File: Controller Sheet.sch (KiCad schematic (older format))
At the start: 20 parts, among them J1 USB_B_Micro, U1 ATSAMD11D14A-SS, Y1 Crystal_GND2

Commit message: Fixed PISO Shift Register Wiring
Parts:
- removed U?: 74HC596, symbol 74xx:74HC596
- removed U?: ADP7142AUJZ-3.3, Package_TO_SOT_SMD:TSOT-23-5, symbol Regulator_Linear:ADP7142AUJZ-3.3
- added U?: AP2138N-3.3TRG1, Package_TO_SOT_SMD:SOT-23_Handsoldering, symbol Library:AP2138N-3.3TRG1
- added U?: 74HC595D_118, digikey-footprints:SOIC-16_W3.90mm, symbol dk_Logic-Shift-Registers:74HC595D_118
- C1, C2, C? (x2): footprint (none) -> Capacitor_SMD:C_1206_3216Metric_Pad1.42x1.75mm_HandSolder
- C?: value 4.7u -> 1u; footprint (none) -> Capacitor_SMD:C_1206_3216Metric_Pad1.42x1.75mm_HandSolder
- C?: value 1n -> 1u; footprint (none) -> Capacitor_SMD:C_1206_3216Metric_Pad1.42x1.75mm_HandSolder
- J1: footprint (none) -> Connector_USB:USB_Micro-B_Molex_47346-0001
- J?: footprint (none) -> Connector_PinHeader_2.54mm:PinHeader_2x04_P2.54mm_Vertical
- J?: footprint (none) -> Connector_PinHeader_1.00mm:PinHeader_1x04_P1.00mm_Vertical
- R? (x3): footprint (none) -> Resistor_SMD:R_1206_3216Metric_Pad1.42x1.75mm_HandSolder
- RV?: footprint (none) -> Potentiometer_THT:Potentiometer_Runtron_RM-065_Vertical
- SW?: footprint (none) -> Button_Switch_THT:SW_PUSH_6mm
- Y1: footprint (none) -> Crystal:Crystal_SMD_SeikoEpson_MC146-4Pin_6.7x1.5mm_HandSoldering; symbol Device:Crystal_GND2 -> Device:Crystal_GND23
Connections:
- net +3V3: now also U?.16 (VCC), U?.2 (OUT)
- net +5V: now also U?.3 (IN)
- net GND: now also U?.1 (GND), U?.13 (OE), U?.8 (GND); no longer Y1.2
- net Lock LEDS/CAPS_LOCK: now also U?.1 (Q1)
- net Lock LEDS/NUM_LOCK: now also U?.15 (Q0)
- net Lock LEDS/SCROLL_LOCK: now also U?.2 (Q2)
- net OUT_SHIFT_0_DATA: now also U?.14 (DS)
- net OUT_SHIFT_RCLK: now also U?.12 (STCP)
- net RESET: now also U?.10 (MR)
- net SHIFT_CLK: now also U?.11 (SHCP)
- net at C4.1, U1.4 (PA08/XIN): now also Y1.4; no longer Y1.3
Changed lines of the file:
@@
 F 0 "J1" H 1657 5067 50  0000 C CNN
 F 1 "USB_B_Micro" H 1657 4976 50  0000 C CNN
-F 2 "" H 1750 4550 50  0001 C CNN
+F 2 "Connector_USB:USB_Micro-B_Molex_47346-0001" H 1750 4550 50  0001 C CNN
 F 3 "~" H 1750 4550 50  0001 C CNN
 	1    1600 4600
@@
 F 0 "C1" H 5715 2796 50  0000 L CNN
 F 1 "100n" H 5715 2705 50  0000 L CNN
-F 2 "" H 5638 2600 50  0001 C CNN
+F 2 "Capacitor_SMD:C_1206_3216Metric_Pad1.42x1.75mm_HandSolder" H 5638 2600 50  0001 C CNN
 F 3 "~" H 5600 2750 50  0001 C CNN
 	1    5600 2750
@@
 F 0 "C2" H 5215 2796 50  0000 L CNN
 F 1 "4.7u" H 5215 2705 50  0000 L CNN
-F 2 "" H 5138 2600 50  0001 C CNN
+F 2 "Capacitor_SMD:C_1206_3216Metric_Pad1.42x1.75mm_HandSolder" H 5138 2600 50  0001 C CNN
 F 3 "~" H 5100 2750 50  0001 C CNN
 	1    5100 2750
@@
 	6750 4300 6750 2600
 $Comp
-L Device:Crystal_GND2 Y1
+L Device:Crystal_GND23 Y1
 U 1 1 5E8CA600
 P 7750 3000
-F 0 "Y1" H 7750 3268 50  0000 C CNN
-F 1 "Crystal_GND2" H 7750 3177 50  0000 C CNN
-F 2 "" H 7750 3000 50  0001 C CNN
+F 0 "Y1" H 7750 3268 50  0000 L CNN
+F 1 "Crystal_GND2" H 7750 3177 50  0000 L CNN
+F 2 "Crystal:Crystal_SMD_SeikoEpson_MC146-4Pin_6.7x1.5mm_HandSoldering" H 7750 3000 50  0001 C CNN
 F 3 "~" H 7750 3000 50  0001 C CNN
 	1    7750 3000
@@
 	8150 3400 7750 3400
 Wire Wire Line
-	7750 3200 7750 3400
-Wire Wire Line
 	7750 3400 7750 3500
 $Comp
@@
 F 0 "SW?" H 10300 4335 50  0000 C CNN
 F 1 "SW_Push" H 10300 4244 50  0000 C CNN
-F 2 "" H 10300 4250 50  0001 C CNN
+F 2 "Button_Switch_THT:SW_PUSH_6mm" H 10300 4250 50  0001 C CNN
 F 3 "~" H 10300 4250 50  0001 C CNN
 	1    10300 4050
@@
 F 0 "R?" H 9270 3546 50  0000 L CNN
 F 1 "100K" H 9270 3455 50  0000 L CNN
-F 2 "" V 9130 3500 50  0001 C CNN
+F 2 "Resistor_SMD:R_1206_3216Metric_Pad1.42x1.75mm_HandSolder" V 9130 3500 50  0001 C CNN
 F 3 "~" H 9200 3500 50  0001 C CNN
 	1    9200 3500
@@
 F 0 "C?" H 9315 4096 50  0000 L CNN
 F 1 "4.7n" H 9315 4005 50  0000 L CNN
-F 2 "" H 9238 3900 50  0001 C CNN
+F 2 "Capacitor_SMD:C_1206_3216Metric_Pad1.42x1.75mm_HandSolder" H 9238 3900 50  0001 C CNN
 F 3 "~" H 9200 4050 50  0001 C CNN
 	1    9200 4050
@@
 F 0 "R?" V 9543 3800 50  0000 C CNN
 F 1 "39" V 9634 3800 50  0000 C CNN
-F 2 "" V 9680 3800 50  0001 C CNN
+F 2 "Resistor_SMD:R_1206_3216Metric_Pad1.42x1.75mm_HandSolder" V 9680 3800 50  0001 C CNN
 F 3 "~" H 9750 3800 50  0001 C CNN
 	1    9750 3800
@@
 F 0 "J?" H 9850 6167 50  0000 C CNN
 F 1 "DEBUG" H 9850 6076 50  0000 C CNN
-F 2 "" H 9800 5750 50  0001 C CNN
+F 2 "Connector_PinHeader_2.54mm:PinHeader_2x04_P2.54mm_Vertical" H 9800 5750 50  0001 C CNN
 F 3 "~" H 9800 5750 50  0001 C CNN
 	1    9800 5750
@@
 OUT_SHIFT_0_DATA
 Wire Wire Line
-	4750 3600 4750 3100
-Wire Wire Line
 	4750 3600 5550 3600
 Wire Wire Line
@@
 F 0 "R?" H 8770 4096 50  0000 L CNN
 F 1 "39" H 8770 4005 50  0000 L CNN
-F 2 "" V 8630 4050 50  0001 C CNN
+F 2 "Resistor_SMD:R_1206_3216Metric_Pad1.42x1.75mm_HandSolder" V 8630 4050 50  0001 C CNN
 F 3 "~" H 8700 4050 50  0001 C CNN
 	1    8700 4050
@@
 P 2900 6150
 F 0 "C?" H 3015 6196 50  0000 L CNN
-F 1 "4.7u" H 3015 6105 50  0000 L CNN
-F 2 "" H 2938 6000 50  0001 C CNN
+F 1 "1u" H 3015 6105 50  0000 L CNN
+F 2 "Capacitor_SMD:C_1206_3216Metric_Pad1.42x1.75mm_HandSolder" H 2938 6000 50  0001 C CNN
 F 3 "~" H 2900 6150 50  0001 C CNN
 	1    2900 6150
 	1    0    0    -1
 $EndComp
-$Comp
-L 74xx:74HC596 U?
-U 1 1 5E946AE2
-P 2850 3300
-F 0 "U?" H 2850 4081 50  0000 C CNN
-F 1 "74HC596" H 2850 3990 50  0000 C CNN
-F 2 "" H 2850 3300 50  0001 C CNN
-F 3 "https://assets.nexperia.com/documents/data-sheet/74HC_HCT595.pdf" H 2850 3300 50  0001 C CNN
-	1    2850 3300
-	-1   0    0    -1
-$EndComp
-Wire Wire Line
-	3250 3100 4750 3100
-Wire Wire Line
-	3950 3400 3250 3400
 Wire Wire Line
 	3950 4400 5550 4400
 Wire Wire Line
-	3850 2900 3250 2900
-Wire Wire Line
 	3850 4500 5550 4500
-Wire Wire Line
-	3250 3500 3500 3500
 $Comp
 L power:GND #PWR?
@@
 $EndComp
 Wire Wire Line
-	3500 3500 3500 4100
-Wire Wire Line
-	2850 4000 2850 4100
-Wire Wire Line
 	2850 4100 3500 4100
 Connection ~ 3500 4100
@@
 F 0 "C?" H 3615 2596 50  0000 L CNN
 F 1 "100n" H 3615 2505 50  0000 L CNN
-F 2 "" H 3538 2400 50  0001 C CNN
+F 2 "Capacitor_SMD:C_1206_3216Metric_Pad1.42x1.75mm_HandSolder" H 3538 2400 50  0001 C CNN
 F 3 "~" H 3500 2550 50  0001 C CNN
 	1    3500 2550
@@
 	2850 2400 3500 2400
 Wire Wire Line
-	3500 2700 3500 3500
-Connection ~ 3500 3500
+	3500 2700 3500 3400
 Wire Wire Line
 	2850 2400 2850 2300
@@
 F 0 "J?" H 1518 5475 50  0000 C CNN
 F 1 "Conn_01x04" H 1518 5566 50  0000 C CNN
-F 2 "" H 1600 5900 50  0001 C CNN
+F 2 "Connector_PinHeader_1.00mm:PinHeader_1x04_P1.00mm_Vertical" H 1600 5900 50  0001 C CNN
 F 3 "~" H 1600 5900 50  0001 C CNN
 	1    1600 5900
@@
 SHIFT_CLK
 Wire Wire Line
-	3950 4400 3950 3400
-Wire Wire Line
-	3850 4500 3850 2900
-Wire Wire Line
-	3250 3200 4850 3200
+	3850 4500 3850 3500
 Wire Wire Line
 	4750 1900 10250 1900
-Connection ~ 4750 3100
 Wire Wire Line
 	4050 4300 4050 1900
@@
 $EndSheet
 Wire Wire Line
-	2450 2900 2100 2900
-Wire Wire Line
-	2450 3000 2100 3000
-Wire Wire Line
-	2450 3100 2100 3100
-$Comp
-L Regulator_Linear:ADP7142AUJZ-3.3 U?
-U 1 1 5EB29370
-P 3500 5800
-F 0 "U?" H 3500 6167 50  0000 C CNN
-F 1 "ADP7142AUJZ-3.3" H 3500 6076 50  0000 C CNN
-F 2 "Package_TO_SOT_SMD:TSOT-23-5" H 3500 5400 50  0001 C CIN
-F 3 "https://www.analog.com/media/en/technical-documentation/data-sheets/ADP7142.pdf" H 3500 5300 50  0001 C CNN
-	1    3500 5800
-	1    0    0    -1
-$EndComp
-Wire Wire Line
 	2150 5700 2900 5700
 Connection ~ 2150 5700
-Wire Wire Line
-	3100 5900 2900 5900
-Wire Wire Line
-	2900 5900 2900 5700
 Connection ~ 2900 5700
 Wire Wire Line
 	2900 5700 3100 5700
-Wire Wire Line
-	2900 5900 2900 6000
-Connection ~ 2900 5900
 Wire Wire Line
 	3500 6100 3500 6300
@@
 Wire Wire Line
 	4100 5500 4100 5700
-Wire Wire Line
-	3900 5800 4100 5800
-Wire Wire Line
-	4100 5800 4100 5700
 Connection ~ 4100 5700
 $Comp
@@
 P 4100 6150
 F 0 "C?" H 4215 6196 50  0000 L CNN
-F 1 "1n" H 4215 6105 50  0000 L CNN
-F 2 "" H 4138 6000 50  0001 C CNN
+F 1 "1u" H 4215 6105 50  0000 L CNN
+F 2 "Capacitor_SMD:C_1206_3216Metric_Pad1.42x1.75mm_HandSolder" H 4138 6000 50  0001 C CNN
 F 3 "~" H 4100 6150 50  0001 C CNN
 	1    4100 6150
 	1    0    0    -1
 $EndComp
-Wire Wire Line
-	4100 5800 4100 6000
-Connection ~ 4100 5800
 $Comp
 L power:GND #PWR?
@@
 Wire Wire Line
 	4650 1800 4650 3700
-Wire Wire Line
-	4750 1900 4750 3100
 Connection ~ 8700 2000
 Wire Wire Line
 	8700 2000 8700 3800
 Wire Wire Line
-	4850 2000 4850 3200
+	4850 2000 4850 3100
 $Comp
 L power:GND #PWR?
@@
 F 0 "RV?" V 7543 1200 50  0000 C CNN
 F 1 "R_POT" V 7634 1200 50  0000 C CNN
-F 2 "" H 7750 1200 50  0001 C CNN
+F 2 "Potentiometer_THT:Potentiometer_Runtron_RM-065_Vertical" H 7750 1200 50  0001 C CNN
 F 3 "~" H 7750 1200 50  0001 C CNN
 	1    7750 1200
@@
 	7500 1500 9250 1500
 Connection ~ 9250 1500
+$Comp
+L Library:AP2138N-3.3TRG1 U?
+U 1 1 5E99716C
+P 3500 5800
+F 0 "U?" H 3500 6167 50  0000 C CNN
+F 1 "AP2138N-3.3TRG1" H 3500 6076 50  0000 C CNN
+F 2 "Package_TO_SOT_SMD:SOT-23_Handsoldering" H 4450 5500 50  0001 C CNN
+F 3 "https://www.diodes.com/assets/Datasheets/AP2138-9.pdf" H 3500 6150 50  0001 C CNN
+	1    3500 5800
+	1    0    0    -1
+$EndComp
+Wire Wire Line
+	2900 5700 2900 6000
+Wire Wire Line
+	4100 5700 4100 6000
+$Comp
+L dk_Logic-Shift-Registers:74HC595D_118 U?
+U 1 1 5E9A4DAC
+P 2850 2800
+F 0 "U?" H 2900 3103 60  0000 C CNN
+F 1 "74HC595D_118" H 2900 2997 60  0000 C CNN
+F 2 "digikey-footprints:SOIC-16_W3.90mm" H 3050 3000 60  0001 L CNN
+F 3 "https://assets.nexperia.com/documents/data-sheet/74HC_HCT595.pdf" H 3050 3100 60  0001 L CNN
+F 4 "1727-2821-1-ND" H 3050 3200 60  0001 L CNN "Digi-Key_PN"
+F 5 "74HC595D,118" H 3050 3300 60  0001 L CNN "MPN"
+F 6 "Integrated Circuits (ICs)" H 3050 3400 60  0001 L CNN "Category"
+F 7 "Logic - Shift Registers" H 3050 3500 60  0001 L CNN "Family"
+F 8 "https://assets.nexperia.com/documents/data-sheet/74HC_HCT595.pdf" H 3050 3600 60  0001 L CNN "DK_Datasheet_Link"
+F 9 "/product-detail/en/nexperia-usa-inc/74HC595D,118/1727-2821-1-ND/763394" H 3050 3700 60  0001 L CNN "DK_Detail_Page"
+F 10 "IC SHIFT REGISTER 8BIT 16SOIC" H 3050 3800 60  0001 L CNN "Description"
+F 11 "Nexperia USA Inc." H 3050 3900 60  0001 L CNN "Manufacturer"
+F 12 "Active" H 3050 4000 60  0001 L CNN "Status"
+	1    2850 2800
+	-1   0    0    -1
+$EndComp
+Wire Wire Line
+	2850 3900 2850 4100
+Wire Wire Line
+	2350 2900 2100 2900
+Wire Wire Line
+	2350 3000 2100 3000
+Wire Wire Line
+	2350 3100 2100 3100
+Wire Wire Line
+	4750 1900 4750 3200
+Wire Wire Line
+	3250 3100 4850 3100
+Wire Wire Line
+	3250 3200 4750 3200
+Connection ~ 4750 3200
+Wire Wire Line
+	4750 3200 4750 3600
+Wire Wire Line
+	3250 3300 3950 3300
+Wire Wire Line
+	3950 3300 3950 4400
+Wire Wire Line
+	3250 3400 3500 3400
+Connection ~ 3500 3400
+Wire Wire Line
+	3500 3400 3500 4100
+Wire Wire Line
+	3250 3500 3850 3500
 $EndSCHEMATC

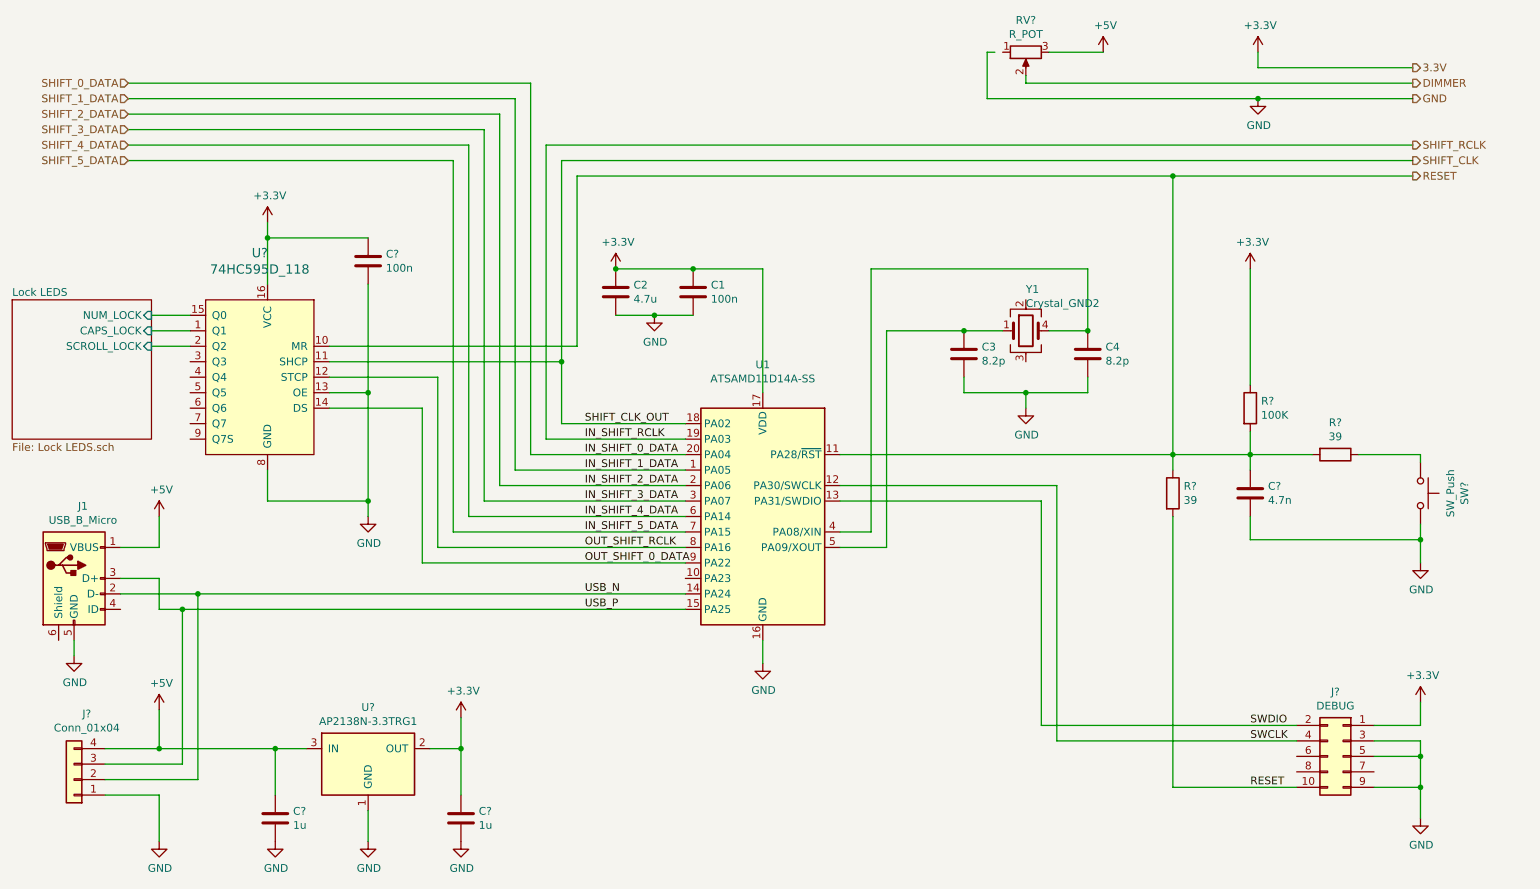
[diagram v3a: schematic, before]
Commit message: Corrected errors found in design rule check
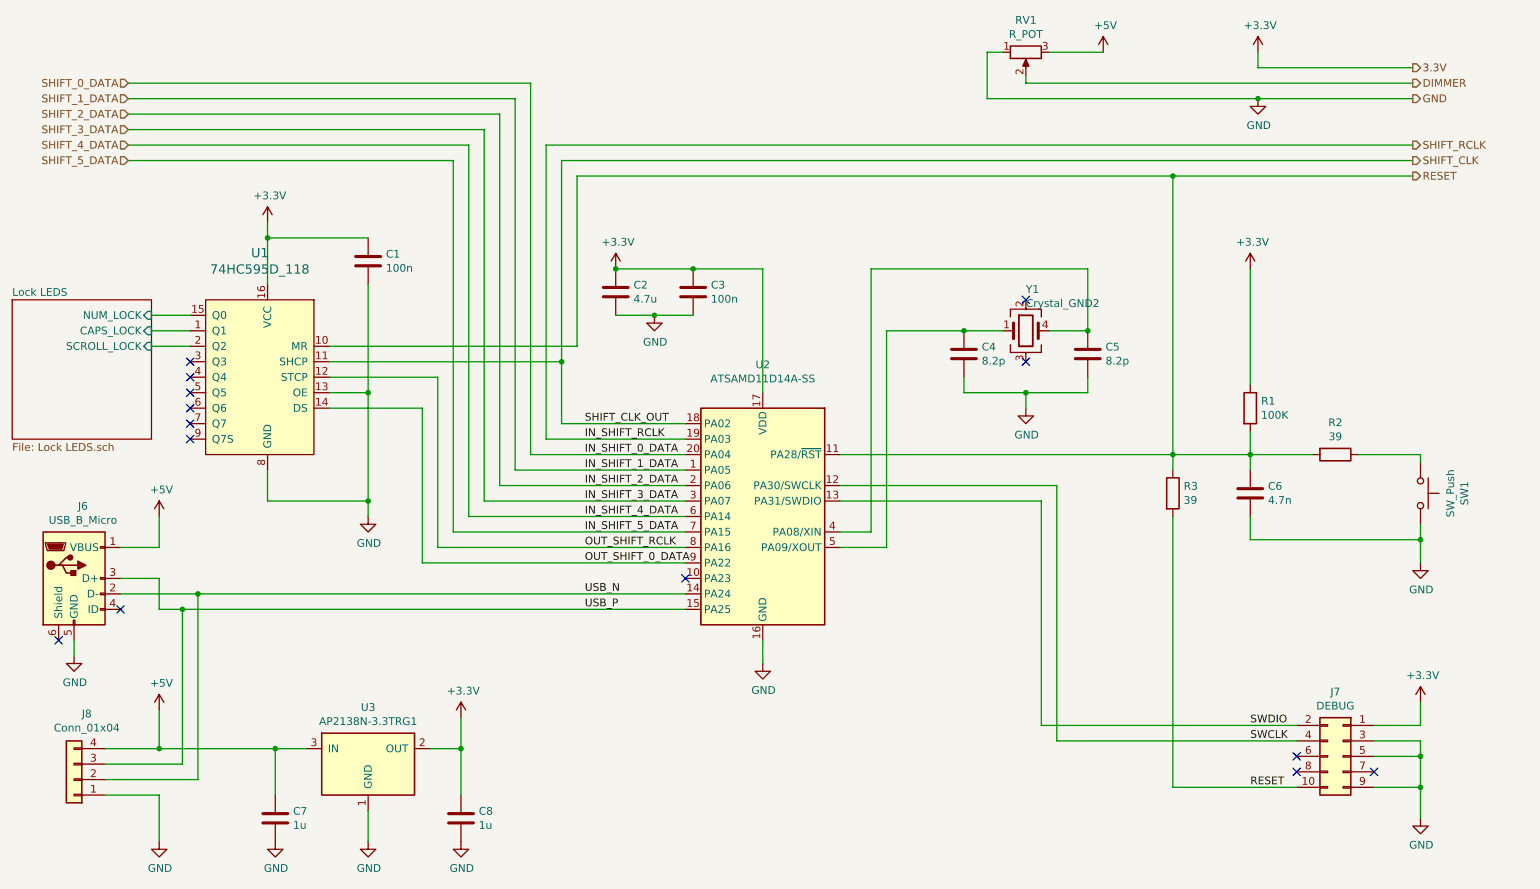
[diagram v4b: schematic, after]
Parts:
- C4: renamed from C3; footprint (none) -> Capacitor_SMD:C_1206_3216Metric_Pad1.42x1.75mm_HandSolder
- C5: renamed from C4; footprint (none) -> Capacitor_SMD:C_1206_3216Metric_Pad1.42x1.75mm_HandSolder
- gave numbers to parts that had none: 13
- renumbered C1 to C3, J1 to J6, U1 to U2
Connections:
- net GND: now also RV1.1
- no-connect marks 0 -> 14

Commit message: Fixed footprint for debug header
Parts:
- J7: footprint Connector_PinHeader_2.54mm:PinHeader_2x04_P2.54mm_Vertical -> Connector_PinHeader_2.54mm:PinHeader_2x05_P2.54mm_Vertical
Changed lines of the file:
@@
 F 0 "J7" H 9850 6167 50  0000 C CNN
 F 1 "DEBUG" H 9850 6076 50  0000 C CNN
-F 2 "Connector_PinHeader_2.54mm:PinHeader_2x04_P2.54mm_Vertical" H 9800 5750 50  0001 C CNN
+F 2 "Connector_PinHeader_2.54mm:PinHeader_2x05_P2.54mm_Vertical" H 9800 5750 50  0001 C CNN
 F 3 "~" H 9800 5750 50  0001 C CNN
 	1    9800 5750

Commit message: Redesigned for single large PCB
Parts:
- J3: renamed from J8; value Conn_01x04 -> USB; footprint Connector_PinHeader_1.00mm:PinHeader_1x04_P1.00mm_Vertical -> Connector_PinHeader_2.54mm:PinHeader_1x04_P2.54mm_Vertical
- renumbered J6 to J1, J7 to J2
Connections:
- net SHIFT_1_DATA is gone; now on net OUT_SHIFT_RCLK: U2.1 (PA05)
- net SHIFT_2_DATA is gone; now on net OUT_SHIFT_0_DATA: U2.2 (PA06)
- net OUT_SHIFT_0_DATA: no longer U2.9 (PA22)
- net OUT_SHIFT_RCLK: no longer U2.8 (PA16)
- net RESET: no longer J2.10 (Pin_10), R3.2
- net SHIFT_0_DATA renamed SHIFT_DATA
- net SHIFT_3_DATA: no longer names the net of U2.3 (PA07)
- net SHIFT_4_DATA: no longer names the net of U2.6 (PA14)
- net SHIFT_5_DATA: no longer names the net of U2.7 (PA15)
- new net RESET_DBG: J2.10 (Pin_10), R3.2
- no-connect marks 14 -> 19
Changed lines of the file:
@@
 $Descr A4 11693 8268
 encoding utf-8
-Sheet 2 18
+Sheet 2 14
 Title ""
 Date ""
@@
 $EndDescr
 $Comp
-L Connector:USB_B_Micro J6
+L Connector:USB_B_Micro J1
 U 1 1 5E8B635B
 P 1600 4600
-F 0 "J6" H 1657 5067 50  0000 C CNN
+F 0 "J1" H 1657 5067 50  0000 C CNN
 F 1 "USB_B_Micro" H 1657 4976 50  0000 C CNN
 F 2 "Connector_USB:USB_Micro-B_Molex_47346-0001" H 1750 4550 50  0001 C CNN
@@
 	6550 4100 7850 4100
 $Comp
-L Connector_Generic:Conn_02x05_Odd_Even J7
+L Connector_Generic:Conn_02x05_Odd_Even J2
 U 1 1 5E8EAF9B
 P 9800 5750
-F 0 "J7" H 9850 6167 50  0000 C CNN
+F 0 "J2" H 9850 6167 50  0000 C CNN
 F 1 "DEBUG" H 9850 6076 50  0000 C CNN
 F 2 "Connector_PinHeader_2.54mm:PinHeader_2x05_P2.54mm_Vertical" H 9800 5750 50  0001 C CNN
@@
 Text Label 9200 5650 0    50   ~ 0
 SWCLK
-Text Label 9200 5950 0    50   ~ 0
-RESET
+Text Label 9000 5950 0    50   ~ 0
+RESET_DBG
 Text Label 4900 4700 0    50   ~ 0
 USB_N
@@
 SHIFT_CLK_OUT
 Text Label 4900 3800 0    50   ~ 0
-IN_SHIFT_0_DATA
+IN_SHIFT_DATA
 Text Label 4900 3900 0    50   ~ 0
-IN_SHIFT_1_DATA
+OUT_SHIFT_RCLK
 Text Label 4900 4000 0    50   ~ 0
-IN_SHIFT_2_DATA
-Text Label 4900 4100 0    50   ~ 0
-IN_SHIFT_3_DATA
-Text Label 4900 4200 0    50   ~ 0
-IN_SHIFT_4_DATA
-Text Label 4900 4300 0    50   ~ 0
-IN_SHIFT_5_DATA
-Text Label 4900 4400 0    50   ~ 0
-OUT_SHIFT_RCLK
-Text Label 4900 4500 0    50   ~ 0
 OUT_SHIFT_0_DATA
 Wire Wire Line
@@
 Wire Wire Line
 	4550 3800 5550 3800
-Wire Wire Line
-	4450 3900 5550 3900
-Wire Wire Line
-	4350 4000 5550 4000
-Wire Wire Line
-	4250 4100 5550 4100
-Wire Wire Line
-	4150 4200 5550 4200
-Wire Wire Line
-	4050 4300 5550 4300
 $Comp
 L Device:R R3
@@
 	1    0    0    -1
 $EndComp
-Wire Wire Line
-	3950 4400 5550 4400
-Wire Wire Line
-	3850 4500 5550 4500
 $Comp
 L power:GND #PWR010
@@
 SHIFT_RCLK
 $Comp
-L Connector_Generic:Conn_01x04 J8
+L Connector_Generic:Conn_01x04 J3
 U 1 1 5E9762B9
 P 1600 5900
-F 0 "J8" H 1518 5475 50  0000 C CNN
-F 1 "Conn_01x04" H 1518 5566 50  0000 C CNN
-F 2 "Connector_PinHeader_1.00mm:PinHeader_1x04_P1.00mm_Vertical" H 1600 5900 50  0001 C CNN
+F 0 "J3" H 1518 5475 50  0000 C CNN
+F 1 "USB" H 1518 5566 50  0000 C CNN
+F 2 "Connector_PinHeader_2.54mm:PinHeader_1x04_P2.54mm_Vertical" H 1600 5900 50  0001 C CNN
 F 3 "~" H 1600 5900 50  0001 C CNN
 	1    1600 5900
@@
 Wire Wire Line
 	2400 4700 5550 4700
-Text HLabel 1950 1400 0    50   Input ~ 0
-SHIFT_0_DATA
-Text HLabel 1950 1500 0    50   Input ~ 0
-SHIFT_1_DATA
-Text HLabel 1950 1600 0    50   Input ~ 0
-SHIFT_2_DATA
-Text HLabel 1950 1700 0    50   Input ~ 0
-SHIFT_3_DATA
 Text HLabel 1950 1800 0    50   Input ~ 0
-SHIFT_4_DATA
-Text HLabel 1950 1900 0    50   Input ~ 0
-SHIFT_5_DATA
+SHIFT_DATA
 Text HLabel 10250 1900 2    50   Output ~ 0
 SHIFT_CLK
 Wire Wire Line
-	3850 4500 3850 3500
-Wire Wire Line
 	4750 1900 10250 1900
 Wire Wire Line
-	4050 4300 4050 1900
-Wire Wire Line
-	4050 1900 1950 1900
-Wire Wire Line
-	4150 4200 4150 1800
-Wire Wire Line
-	4150 1800 1950 1800
-Wire Wire Line
-	4250 1700 1950 1700
-Wire Wire Line
-	4250 1700 4250 4100
-Wire Wire Line
-	4350 4000 4350 1600
-Wire Wire Line
-	4350 1600 1950 1600
-Wire Wire Line
-	4450 3900 4450 1500
-Wire Wire Line
-	4450 1500 1950 1500
-Wire Wire Line
-	4550 3800 4550 1400
-Wire Wire Line
-	4550 1400 1950 1400
+	4550 1800 1950 1800
 Wire Wire Line
 	4850 2000 8700 2000
@@
 	3250 3300 3950 3300
 Wire Wire Line
-	3950 3300 3950 4400
-Wire Wire Line
 	3250 3400 3500 3400
 Connection ~ 3500 3400
@@
 NoConn ~ 2350 3300
 NoConn ~ 2350 3200
+Wire Wire Line
+	3850 4000 5550 4000
+Wire Wire Line
+	3950 3900 5550 3900
+Wire Wire Line
+	3950 3900 3950 3300
+Wire Wire Line
+	3850 3500 3850 4000
+Wire Wire Line
+	4550 1800 4550 3800
+NoConn ~ 5550 4500
+NoConn ~ 5550 4400
+NoConn ~ 5550 4300
+NoConn ~ 5550 4200
+NoConn ~ 5550 4100
 $EndSCHEMATC
